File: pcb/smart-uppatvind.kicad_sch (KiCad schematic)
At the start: 63 parts, among them J1 PWR, J2 EXT_SENSOR, J3 UART_PROG, J4 FAN, Q1 IRLML9301, Q2 MMBT3904, Q3 MMBT3904, Q4 MMBT3904, Q5 Q_NMOS_GSD, SW1 EN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

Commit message: Adjusted MCU pin assignment, progressed with power routing
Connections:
- net FAN_EN: now also U3.5 (IO6); no longer U3.10 (IO10)
- net GND: now also C5.2
- net GNDPWR: no longer C5.2
- net PWM: now also U3.6 (IO7); no longer U3.16 (IO2)
- net SCL: now also U3.16 (IO2); no longer U3.6 (IO7)
- net SDA: now also U3.17 (IO1); no longer U3.5 (IO6)
- net at JP1.2 (B): now also U3.10 (IO10); no longer U3.17 (IO1)
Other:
- moved on the sheet: JP1
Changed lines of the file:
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@@
 	)
 	(junction
-		(at 105.41 43.18)
-		(diameter 0)
-		(color 0 0 0 0)
-	)
-	(junction
 		(at 212.09 25.4)
 		(diameter 0)
@@
 	(wire
 		(pts
-			(xy 29.21 114.3) (xy 31.75 114.3)
+			(xy 39.37 137.16) (xy 41.91 137.16)
 		)
 		(stroke
@@
 	(wire
 		(pts
-			(xy 39.37 137.16) (xy 52.07 137.16)
-		)
-		(stroke
-			(width 0)
-			(type default)
-		)
-	)
-	(wire
-		(pts
 			(xy 40.64 49.53) (xy 40.64 52.07)
 		)
@@
 	(wire
 		(pts
-			(xy 39.37 116.84) (xy 52.07 116.84)
-		)
-		(stroke
-			(width 0)
-			(type default)
-		)
-	)
-	(wire
-		(pts
 			(xy 95.25 176.53) (xy 104.14 176.53)
 		)
@@
 	(wire
 		(pts
-			(xy 97.79 43.18) (xy 105.41 43.18)
-		)
-		(stroke
-			(width 0)
-			(type default)
-		)
-	)
-	(wire
-		(pts
 			(xy 95.25 173.99) (xy 104.14 173.99)
 		)
@@
 	(wire
 		(pts
-			(xy 105.41 43.18) (xy 113.03 43.18)
+			(xy 162.56 25.4) (xy 184.15 25.4)
 		)
 		(stroke
@@
 	(wire
 		(pts
-			(xy 162.56 25.4) (xy 184.15 25.4)
+			(xy 196.85 113.03) (xy 196.85 111.76)
 		)
 		(stroke
@@
 	(wire
 		(pts
-			(xy 196.85 113.03) (xy 196.85 111.76)
+			(xy 59.69 22.86) (xy 59.69 26.67)
 		)
 		(stroke
@@
 	(wire
 		(pts
-			(xy 59.69 22.86) (xy 59.69 26.67)
+			(xy 39.37 129.54) (xy 52.07 129.54)
 		)
 		(stroke
@@
 	(wire
 		(pts
-			(xy 39.37 114.3) (xy 52.07 114.3)
-		)
-		(stroke
-			(width 0)
-			(type default)
-		)
-	)
-	(wire
-		(pts
 			(xy 257.81 25.4) (xy 269.24 25.4)
 		)
@@
 	(wire
 		(pts
+			(xy 49.53 137.16) (xy 52.07 137.16)
+		)
+		(stroke
+			(width 0)
+			(type default)
+		)
+	)
+	(wire
+		(pts
 			(xy 212.09 30.48) (xy 212.09 36.83)
 		)
@@
 	(wire
 		(pts
-			(xy 39.37 129.54) (xy 52.07 129.54)
-		)
-		(stroke
-			(width 0)
-			(type default)
-		)
-	)
-	(wire
-		(pts
 			(xy 278.13 138.43) (xy 278.13 143.51)
 		)
@@
 	(wire
 		(pts
-			(xy 113.03 38.1) (xy 113.03 43.18)
+			(xy 113.03 38.1) (xy 113.03 55.88)
 		)
 		(stroke
@@
 	(wire
 		(pts
+			(xy 39.37 114.3) (xy 52.07 114.3)
+		)
+		(stroke
+			(width 0)
+			(type default)
+		)
+	)
+	(wire
+		(pts
 			(xy 243.84 138.43) (xy 247.65 138.43)
 		)
@@
 	(wire
 		(pts
+			(xy 113.03 55.88) (xy 125.73 55.88)
+		)
+		(stroke
+			(width 0)
+			(type default)
+		)
+	)
+	(wire
+		(pts
 			(xy 123.19 107.95) (xy 139.7 107.95)
 		)
@@
 	(wire
 		(pts
-			(xy 105.41 43.18) (xy 105.41 46.99)
-		)
-		(stroke
-			(width 0)
-			(type default)
-		)
-	)
-	(wire
-		(pts
 			(xy 170.18 125.73) (xy 161.29 125.73)
 		)
@@
 	(wire
 		(pts
-			(xy 39.37 127) (xy 52.07 127)
-		)
-		(stroke
-			(width 0)
-			(type default)
-		)
-	)
-	(wire
-		(pts
 			(xy 96.52 130.81) (xy 105.41 130.81)
 		)
@@
 	(wire
 		(pts
+			(xy 39.37 127) (xy 52.07 127)
+		)
+		(stroke
+			(width 0)
+			(type default)
+		)
+	)
+	(wire
+		(pts
 			(xy 262.89 143.51) (xy 259.08 143.51)
 		)
@@
 	(wire
 		(pts
+			(xy 39.37 116.84) (xy 52.07 116.84)
+		)
+		(stroke
+			(width 0)
+			(type default)
+		)
+	)
+	(wire
+		(pts
 			(xy 151.13 170.18) (xy 151.13 171.45)
 		)
@@
 	)
 	(label "FAN_EN"
-		(at 39.37 137.16 0)
+		(at 39.37 127 0)
 		(fields_autoplaced yes)
 		(effects
@@
 	)
 	(label "FG"
-		(at 29.21 114.3 0)
+		(at 39.37 137.16 0)
 		(fields_autoplaced yes)
 		(effects
@@
 	)
 	(label "SCL"
-		(at 39.37 129.54 0)
+		(at 39.37 116.84 0)
 		(fields_autoplaced yes)
 		(effects
@@
 	)
 	(label "PWM"
-		(at 39.37 116.84 0)
+		(at 39.37 129.54 0)
 		(fields_autoplaced yes)
 		(effects
@@
 	)
 	(label "SDA"
-		(at 39.37 127 0)
+		(at 39.37 114.3 0)
 		(fields_autoplaced yes)
 		(effects
@@
 	(symbol
 		(lib_id "Jumper:SolderJumper_2_Open")
-		(at 35.56 114.3 0)
+		(at 45.72 137.16 0)
 		(unit 1)
 		(exclude_from_sim yes)
@@
 		(fields_autoplaced yes)
 		(property "Reference" "JP1"
-			(at 35.56 110.49 0)
+			(at 45.72 133.35 0)
 			(effects
 				(font
@@
 		)
 		(property "Value" "SolderJumper_2_Open"
-			(at 35.56 110.49 0)
+			(at 45.72 133.35 0)
 			(effects
 				(font
@@
 		)
 		(property "Footprint" "Jumper:SolderJumper-2_P1.3mm_Open_RoundedPad1.0x1.5mm"
-			(at 35.56 114.3 0)
+			(at 45.72 137.16 0)
 			(effects
 				(font
@@
 		)
 		(property "Datasheet" "~"
-			(at 35.56 114.3 0)
+			(at 45.72 137.16 0)
 			(effects
 				(font
@@
 		)
 		(property "Description" "Solder Jumper, 2-pole, open"
-			(at 35.56 114.3 0)
+			(at 45.72 137.16 0)
 			(effects
 				(font
@@
 	(symbol
 		(lib_id "power:GNDPWR")
-		(at 105.41 46.99 0)
+		(at 97.79 43.18 0)
 		(unit 1)
 		(exclude_from_sim no)
@@
 		(fields_autoplaced yes)
 		(property "Reference" "#PWR011"
-			(at 105.41 52.07 0)
+			(at 97.79 48.26 0)
 			(effects
 				(font
@@
 		)
 		(property "Value" "GNDPWR"
-			(at 105.283 50.8 0)
+			(at 97.663 46.99 0)
 			(effects
 				(font
@@
 		)
 		(property "Footprint" ""
-			(at 105.41 48.26 0)
+			(at 97.79 44.45 0)
 			(effects
 				(font
@@
 		)
 		(property "Datasheet" ""
-			(at 105.41 48.26 0)
+			(at 97.79 44.45 0)
 			(effects
 				(font
@@
 		)
 		(property "Description" "Power symbol creates a global label with name \"GNDPWR\" , global ground"
-			(at 105.41 46.99 0)
+			(at 97.79 43.18 0)
 			(effects
 				(font

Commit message: Adjusted layout
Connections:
- net SW_FILTER: now also U3.10 (IO10); no longer U3.3 (IO4)
- net at JP1.2 (B): now also U3.3 (IO4); no longer U3.10 (IO10)
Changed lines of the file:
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@@
 	(wire
 		(pts
-			(xy 39.37 137.16) (xy 41.91 137.16)
-		)
-		(stroke
-			(width 0)
-			(type default)
-		)
-	)
-	(wire
-		(pts
 			(xy 36.83 176.53) (xy 48.26 176.53)
 		)
@@
 	(wire
 		(pts
+			(xy 39.37 137.16) (xy 52.07 137.16)
+		)
+		(stroke
+			(width 0)
+			(type default)
+		)
+	)
+	(wire
+		(pts
 			(xy 250.19 40.64) (xy 250.19 45.72)
 		)
@@
 	(wire
 		(pts
-			(xy 49.53 137.16) (xy 52.07 137.16)
+			(xy 39.37 121.92) (xy 52.07 121.92)
 		)
 		(stroke
@@
 	(wire
 		(pts
-			(xy 39.37 121.92) (xy 52.07 121.92)
-		)
-		(stroke
-			(width 0)
-			(type default)
-		)
-	)
-	(wire
-		(pts
 			(xy 123.19 142.24) (xy 113.03 142.24)
 		)
@@
 	(wire
 		(pts
+			(xy 27.94 121.92) (xy 31.75 121.92)
+		)
+		(stroke
+			(width 0)
+			(type default)
+		)
+	)
+	(wire
+		(pts
 			(xy 31.75 57.15) (xy 36.83 57.15)
 		)
@@
 		)
 	)
+	(label "FG"
+		(at 27.94 121.92 0)
+		(fields_autoplaced yes)
+		(effects
+			(font
+				(size 1.27 1.27)
+			)
+			(justify left bottom)
+		)
+	)
 	(label "PWM"
 		(at 128.27 177.8 0)
@@
 		)
 	)
-	(label "FG"
-		(at 39.37 137.16 0)
-		(fields_autoplaced yes)
-		(effects
-			(font
-				(size 1.27 1.27)
-			)
-			(justify left bottom)
-		)
-	)
 	(label "RTS"
 		(at 161.29 128.27 0)
@@
 	)
 	(label "SW_FILTER"
-		(at 39.37 121.92 0)
+		(at 39.37 137.16 0)
 		(fields_autoplaced yes)
 		(effects
@@
 	)
 	(symbol
-		(lib_id "power:VDD")
-		(at 59.69 22.86 0)
+		(lib_id "Jumper:SolderJumper_2_Open")
+		(at 35.56 121.92 0)
 		(unit 1)
-		(exclude_from_sim no)
-		(in_bom yes)
+		(exclude_from_sim yes)
+		(in_bom no)
 		(on_board yes)
 		(dnp no)
-		(fields_autoplaced yes)
-		(property "Reference" "#PWR06"
-			(at 59.69 26.67 0)
+		(property "Reference" "JP1"
+			(at 35.56 119.38 0)
 			(effects
 				(font
 					(size 1.27 1.27)
 				)
-				(hide yes)
 			)
 		)
-		(property "Value" "VDD"
-			(at 59.69 17.78 0)
+		(property "Value" "SolderJumper_2_Open"
+			(at 35.56 118.11 0)
 			(effects
 				(font
 					(size 1.27 1.27)
 				)
+				(hide yes)
 			)
 		)
-		(property "Footprint" ""
-			(at 59.69 22.86 0)
+		(property "Footprint" "Jumper:SolderJumper-2_P1.3mm_Open_RoundedPad1.0x1.5mm"
+			(at 35.56 121.92 0)
 			(effects
 				(font
@@
 			)
 		)
-		(property "Datasheet" ""
-			(at 59.69 22.86 0)
+		(property "Datasheet" "~"
+			(at 35.56 121.92 0)
 			(effects
 				(font
@@
 			)
 		)
-		(property "Description" "Power symbol creates a global label with name \"VDD\""
-			(at 59.69 22.86 0)
+		(property "Description" "Solder Jumper, 2-pole, open"
+			(at 35.56 121.92 0)
 			(effects
 				(font
@@
 			)
 		)
+		(pin "2"
+		)
 		(pin "1"
 		)
@@
 			(project "smart-uppatvind"
 				(path "/b09dc29a-b779-491f-be6b-b7a621e0664e"
-					(reference "#PWR06")
+					(reference "JP1")
 					(unit 1)
 				)
@@
 	)
 	(symbol
-		(lib_id "Jumper:SolderJumper_2_Open")
-		(at 45.72 137.16 0)
+		(lib_id "power:VDD")
+		(at 59.69 22.86 0)
 		(unit 1)
-		(exclude_from_sim yes)
-		(in_bom no)
+		(exclude_from_sim no)
+		(in_bom yes)
 		(on_board yes)
 		(dnp no)
 		(fields_autoplaced yes)
-		(property "Reference" "JP1"
-			(at 45.72 133.35 0)
+		(property "Reference" "#PWR06"
+			(at 59.69 26.67 0)
 			(effects
 				(font
 					(size 1.27 1.27)
 				)
+				(hide yes)
 			)
 		)
-		(property "Value" "SolderJumper_2_Open"
-			(at 45.72 133.35 0)
+		(property "Value" "VDD"
+			(at 59.69 17.78 0)
 			(effects
 				(font
 					(size 1.27 1.27)
 				)
-				(hide yes)
 			)
 		)
-		(property "Footprint" "Jumper:SolderJumper-2_P1.3mm_Open_RoundedPad1.0x1.5mm"
-			(at 45.72 137.16 0)
+		(property "Footprint" ""
+			(at 59.69 22.86 0)
 			(effects
 				(font
@@
 			)
 		)
-		(property "Datasheet" "~"
-			(at 45.72 137.16 0)
+		(property "Datasheet" ""
+			(at 59.69 22.86 0)
 			(effects
 				(font
@@
 			)
 		)
-		(property "Description" "Solder Jumper, 2-pole, open"
-			(at 45.72 137.16 0)
+		(property "Description" "Power symbol creates a global label with name \"VDD\""
+			(at 59.69 22.86 0)
 			(effects
 				(font
@@
 			)
 		)
-		(pin "2"
-		)
 		(pin "1"
 		)
 		(instances
-			(project ""
+			(project "smart-uppatvind"
 				(path "/b09dc29a-b779-491f-be6b-b7a621e0664e"
-					(reference "JP1")
+					(reference "#PWR06")
 					(unit 1)
 				)

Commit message: Minor adjustments, added missing 3D models
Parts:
- J2: value EXT_SENSOR -> QWIIC
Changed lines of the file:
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@@
 			)
 		)
-		(property "Value" "EXT_SENSOR"
+		(property "Value" "QWIIC"
 			(at 71.12 29.5655 0)
 			(effects

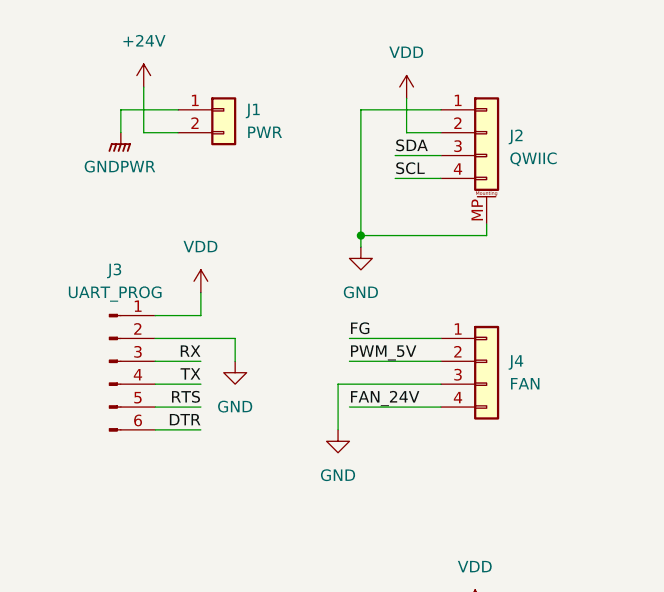
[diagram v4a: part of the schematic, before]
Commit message: Fixed inverted signals on main connectors, added generated schematic
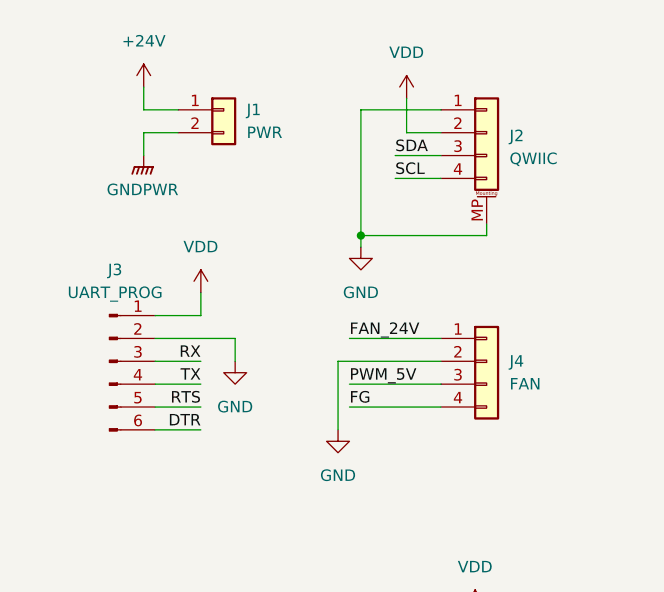
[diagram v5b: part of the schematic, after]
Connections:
- net +24V: now also J1.1 (Pin_1); no longer J1.2 (Pin_2)
- net FAN_24V: now also J4.1 (Pin_1); no longer J4.4 (Pin_4)
- net FG: now also J4.4 (Pin_4); no longer J4.1 (Pin_1)
- net GND: now also J4.2 (Pin_2); no longer J4.3 (Pin_3)
- net GNDPWR: now also J1.2 (Pin_2); no longer J1.1 (Pin_1)
- net PWM_5V: now also J4.3 (Pin_3); no longer J4.2 (Pin_2)
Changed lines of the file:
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@@
 	(wire
 		(pts
-			(xy 52.07 54.61) (xy 52.07 59.69)
+			(xy 52.07 52.07) (xy 63.5 52.07)
 		)
 		(stroke
@@
 	(wire
 		(pts
+			(xy 30.48 26.67) (xy 34.29 26.67)
+		)
+		(stroke
+			(width 0)
+			(type default)
+		)
+	)
+	(wire
+		(pts
 			(xy 259.08 138.43) (xy 261.62 138.43)
 		)
@@
 	(wire
 		(pts
+			(xy 30.48 29.21) (xy 30.48 26.67)
+		)
+		(stroke
+			(width 0)
+			(type default)
+		)
+	)
+	(wire
+		(pts
 			(xy 95.25 176.53) (xy 104.14 176.53)
 		)
@@
 	(wire
 		(pts
-			(xy 53.34 52.07) (xy 63.5 52.07)
-		)
-		(stroke
-			(width 0)
-			(type default)
-		)
-	)
-	(wire
-		(pts
 			(xy 182.88 135.89) (xy 184.15 135.89)
 		)
@@
 	(wire
 		(pts
-			(xy 30.48 26.67) (xy 34.29 26.67)
-		)
-		(stroke
-			(width 0)
-			(type default)
-		)
-	)
-	(wire
-		(pts
 			(xy 271.78 138.43) (xy 278.13 138.43)
 		)
@@
 	(wire
 		(pts
-			(xy 30.48 21.59) (xy 30.48 26.67)
-		)
-		(stroke
-			(width 0)
-			(type default)
-		)
-	)
-	(wire
-		(pts
 			(xy 205.74 121.92) (xy 209.55 121.92)
 		)
@@
 	(wire
 		(pts
+			(xy 30.48 24.13) (xy 34.29 24.13)
+		)
+		(stroke
+			(width 0)
+			(type default)
+		)
+	)
+	(wire
+		(pts
 			(xy 36.83 46.99) (xy 31.75 46.99)
 		)
@@
 	(wire
 		(pts
-			(xy 27.94 26.67) (xy 27.94 24.13)
+			(xy 52.07 52.07) (xy 52.07 59.69)
 		)
 		(stroke
@@
 	(wire
 		(pts
+			(xy 30.48 21.59) (xy 30.48 24.13)
+		)
+		(stroke
+			(width 0)
+			(type default)
+		)
+	)
+	(wire
+		(pts
 			(xy 95.25 109.22) (xy 101.6 109.22)
 		)
@@
 	(wire
 		(pts
-			(xy 52.07 54.61) (xy 63.5 54.61)
-		)
-		(stroke
-			(width 0)
-			(type default)
-		)
-	)
-	(wire
-		(pts
 			(xy 243.84 113.03) (xy 247.65 113.03)
 		)
@@
 	(wire
 		(pts
-			(xy 27.94 24.13) (xy 34.29 24.13)
-		)
-		(stroke
-			(width 0)
-			(type default)
-		)
-	)
-	(wire
-		(pts
 			(xy 39.37 124.46) (xy 52.07 124.46)
 		)
@@
 	(wire
 		(pts
+			(xy 53.34 54.61) (xy 63.5 54.61)
+		)
+		(stroke
+			(width 0)
+			(type default)
+		)
+	)
+	(wire
+		(pts
 			(xy 29.21 185.42) (xy 29.21 187.96)
 		)
@@
 	)
 	(label "PWM_5V"
-		(at 53.34 52.07 0)
+		(at 53.34 54.61 0)
 		(fields_autoplaced yes)
 		(effects
@@
 	)
 	(label "FG"
-		(at 53.34 49.53 0)
+		(at 53.34 57.15 0)
 		(fields_autoplaced yes)
 		(effects
@@
 	)
 	(label "FAN_24V"
-		(at 53.34 57.15 0)
+		(at 53.34 49.53 0)
 		(fields_autoplaced yes)
 		(effects
@@
 	(symbol
 		(lib_id "power:GNDPWR")
-		(at 27.94 26.67 0)
+		(at 30.48 29.21 0)
 		(unit 1)
 		(exclude_from_sim no)
@@
 		(fields_autoplaced yes)
 		(property "Reference" "#PWR07"
-			(at 27.94 31.75 0)
+			(at 30.48 34.29 0)
 			(effects
 				(font
@@
 		)
 		(property "Value" "GNDPWR"
-			(at 27.813 30.48 0)
+			(at 30.353 33.02 0)
 			(effects
 				(font
@@
 		)
 		(property "Footprint" ""
-			(at 27.94 27.94 0)
+			(at 30.48 30.48 0)
 			(effects
 				(font
@@
 		)
 		(property "Datasheet" ""
-			(at 27.94 27.94 0)
+			(at 30.48 30.48 0)
 			(effects
 				(font
@@
 		)
 		(property "Description" "Power symbol creates a global label with name \"GNDPWR\" , global ground"
-			(at 27.94 26.67 0)
+			(at 30.48 29.21 0)
 			(effects
 				(font

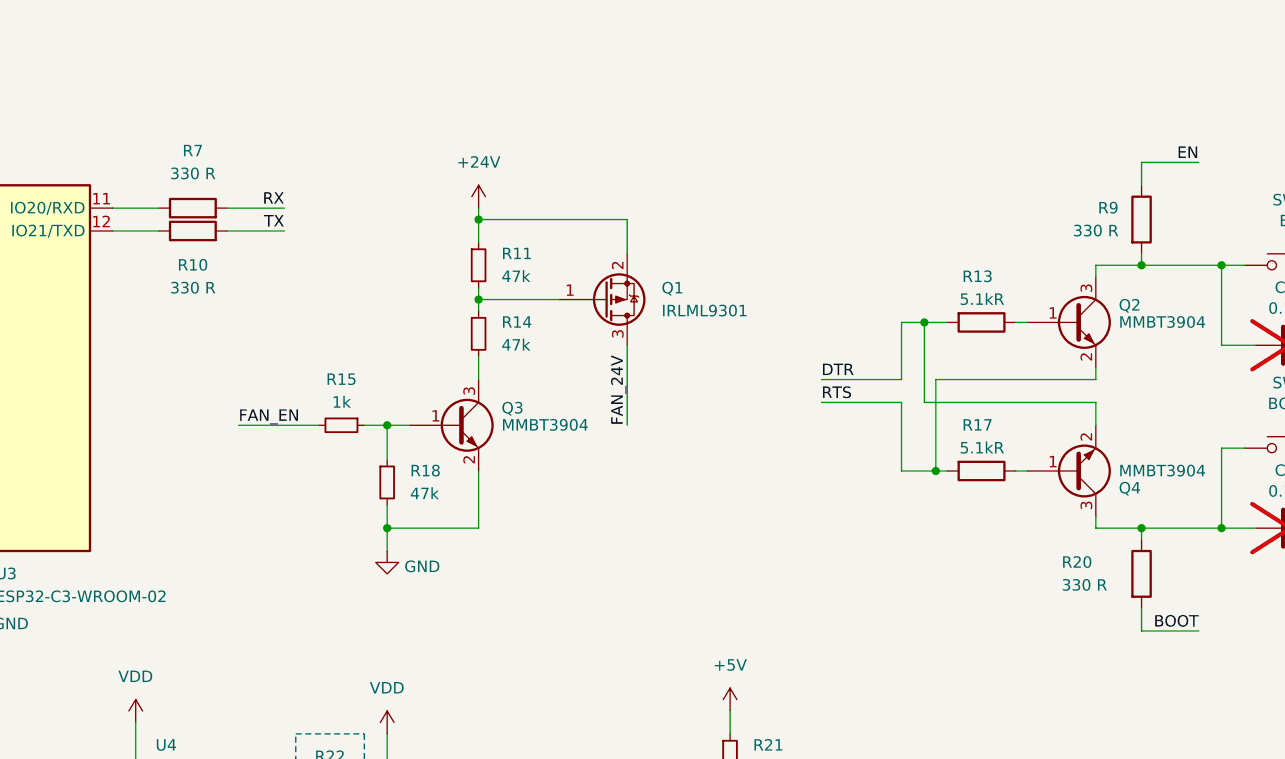
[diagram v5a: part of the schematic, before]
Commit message: Formatted some resistor values
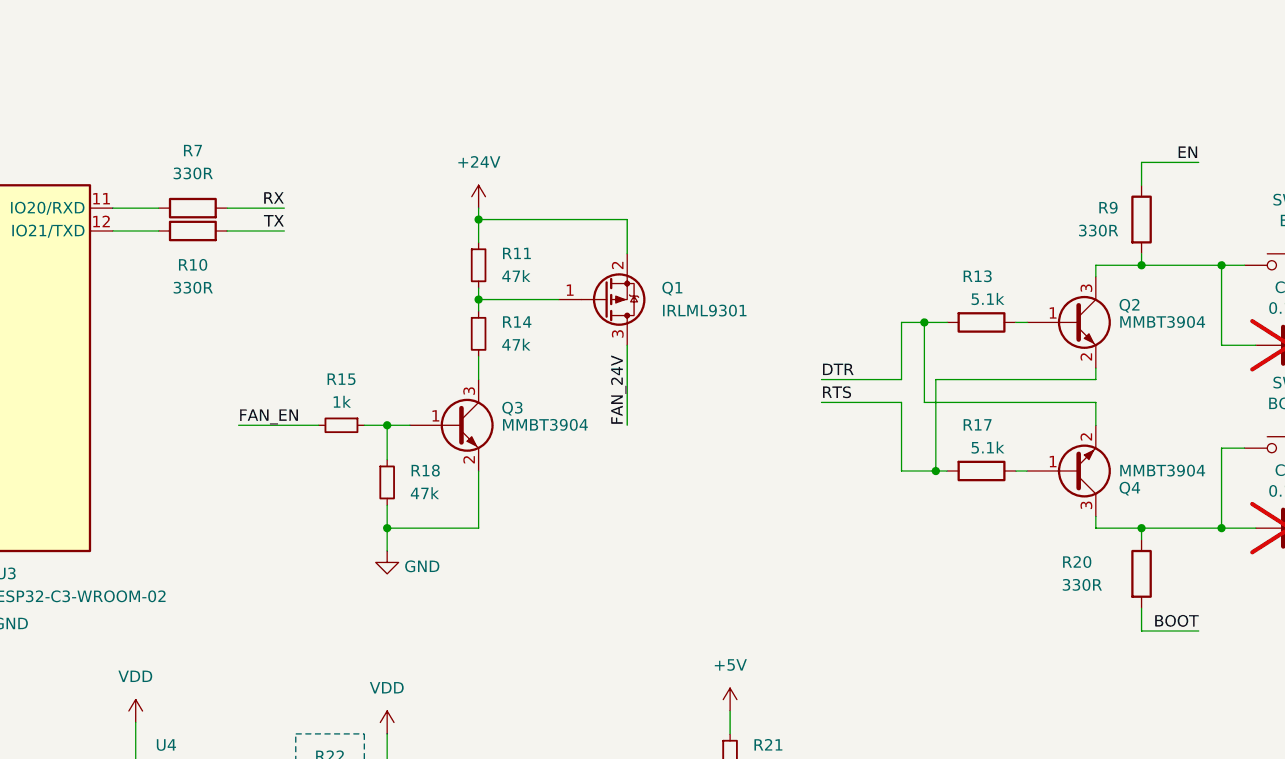
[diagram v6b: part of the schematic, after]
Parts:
- R10, R20, R7, R9: value 330 R -> 330R
- R13, R17: value 5.1kR -> 5.1k
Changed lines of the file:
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@@
 			)
 		)
-		(property "Value" "330 R"
+		(property "Value" "330R"
 			(at 91.44 115.57 90)
 			(effects
@@
 			)
 		)
-		(property "Value" "330 R"
+		(property "Value" "330R"
 			(at 91.44 102.87 90)
 			(effects
@@
 			)
 		)
-		(property "Value" "5.1kR"
+		(property "Value" "5.1k"
 			(at 181.61 116.84 90)
 			(effects
@@
 			)
 		)
-		(property "Value" "330 R"
+		(property "Value" "330R"
 			(at 187.96 148.59 0)
 			(effects
@@
 			)
 		)
-		(property "Value" "5.1kR"
+		(property "Value" "5.1k"
 			(at 181.61 133.35 90)
 			(effects
@@
 			)
 		)
-		(property "Value" "330 R"
+		(property "Value" "330R"
 			(at 194.31 109.2199 0)
 			(effects
